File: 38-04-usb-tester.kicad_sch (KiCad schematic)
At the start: 63 parts, among them J1 Conn_1x05, J2 USB_C_12401832E402A, J3 USB_C_12401832E402A, J4 USB_Micro-B_KH-MICRO5P-JN, J5 USB_Mini-B_U-M-M5DD-W-1, J6 USB3_A_HC-USB3.0-L168-WP, SW1 SW_SPDT, SW2 ZX-1.27BM-4PSMD, U1 STM32C031K6Tx

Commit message: added defaults for jlpcb, fixed usb schematics
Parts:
- R1, R2, R3: footprint Resistor_SMD:R_0201_0603Metric -> Resistor_SMD:R_0805_2012Metric_Pad1.20x1.40mm_HandSolder; JLPCB_MPN 🔶TBD -> DNP; JLPCB_Mfg 🔶TBD -> DNP; JLPCB_Part_No 🔶TBD -> DNP; JLPCB_Price 🔶TBD -> DNP
- R5: footprint Resistor_SMD:R_0201_0603Metric -> Resistor_SMD:R_0805_2012Metric_Pad1.20x1.40mm_HandSolder
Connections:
- net GND: no longer J3.A1 (GND_A1), J3.A12 (GND_A12), J3.B12 (GND_B12)
- net B_GND_B1 renamed B_GND_A1
- net B_GND_A1: now also J3.A1 (GND_A1), J3.A12 (GND_A12), J3.B12 (GND_B12)
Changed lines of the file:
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@@
   (junction (at 334.01 184.785) (diameter 0) (color 0 0 0 0)
   )
+  (junction (at 128.27 173.99) (diameter 0) (color 0 0 0 0)
+  )
   (junction (at 31.75 180.975) (diameter 0) (color 0 0 0 0)
   )
+  (junction (at 128.27 171.45) (diameter 0) (color 0 0 0 0)
+  )
   (junction (at 223.52 57.785) (diameter 0) (color 0 0 0 0)
   )
@@
     (stroke (width 0) (type default))
   )
+  (wire (pts (xy 128.27 171.45) (xy 128.27 168.91))
+    (stroke (width 0) (type default))
+  )
   (wire (pts (xy 281.305 185.42) (xy 274.955 185.42))
     (stroke (width 0) (type default))
@@
     (stroke (width 0) (type default))
   )
+  (wire (pts (xy 128.27 173.99) (xy 139.065 173.99))
+    (stroke (width 0) (type default))
+  )
   (wire (pts (xy 29.845 126.365) (xy 41.275 126.365))
     (stroke (width 0) (type default))
   )
+  (wire (pts (xy 116.205 168.91) (xy 128.27 168.91))
+    (stroke (width 0) (type default))
+  )
   (wire (pts (xy 60.96 234.95) (xy 60.96 231.775))
     (stroke (width 0) (type default))
@@
     (stroke (width 0) (type default))
   )
+  (wire (pts (xy 128.27 171.45) (xy 128.27 173.99))
+    (stroke (width 0) (type default))
+  )
   (wire (pts (xy 203.835 142.24) (xy 203.835 144.78))
     (stroke (width 0) (type default))
@@
     (stroke (width 0) (type default))
   )
+  (wire (pts (xy 116.205 171.45) (xy 128.27 171.45))
+    (stroke (width 0) (type default))
+  )
   (wire (pts (xy 130.81 32.385) (xy 143.51 32.385))
     (stroke (width 0) (type default))
@@
     (stroke (width 0) (type default))
   )
+  (wire (pts (xy 116.205 173.99) (xy 128.27 173.99))
+    (stroke (width 0) (type default))
+  )
   (wire (pts (xy 215.9 139.7) (xy 218.44 139.7))
     (stroke (width 0) (type default))
@@
     (effects (font (size 1.27 1.27)) (justify right bottom))
   )
+  (label "B_GND_B1" (at 139.065 173.99 180) (fields_autoplaced)
+    (effects (font (size 1.27 1.27)) (justify right bottom))
+  )
   (label "A_SBU2" (at 88.9 118.745 180) (fields_autoplaced)
     (effects (font (size 1.27 1.27)) (justify right bottom))
@@
     (effects (font (size 1.27 1.27)) (justify left bottom))
   )
+  (label "B_GND_B12" (at 116.205 173.99 0) (fields_autoplaced)
+    (effects (font (size 1.27 1.27)) (justify left bottom))
+  )
   (label "ID" (at 285.115 191.77 180) (fields_autoplaced)
     (effects (font (size 1.27 1.27)) (justify right bottom))
@@
     (effects (font (size 1.27 1.27)) (justify left bottom))
   )
+  (label "B_GND_A1" (at 116.205 168.91 0) (fields_autoplaced)
+    (effects (font (size 1.27 1.27)) (justify left bottom))
+  )
   (label "CC_bb" (at 260.35 165.735 180) (fields_autoplaced)
     (effects (font (size 1.27 1.27)) (justify right bottom))
@@
     (effects (font (size 1.27 1.27)) (justify left bottom))
   )
+  (label "B_GND_A12" (at 116.205 171.45 0) (fields_autoplaced)
+    (effects (font (size 1.27 1.27)) (justify left bottom))
+  )
   (label "B_CC1_SENS" (at 184.785 42.545 180) (fields_autoplaced)
     (effects (font (size 1.27 1.27)) (justify right bottom))
@@
     )
   )
-  (symbol (lib_name "GND_1") (lib_id "power:GND") (at 135.255 157.48 0) (unit 1)
-    (in_bom yes) (on_board yes) (dnp no)
-    (property "Reference" "#PWR020" (at 135.255 163.83 0)
-      (effects (font (size 1.27 1.27)) hide)
-    )
-    (property "Value" "GND" (at 135.255 161.29 0)
-      (effects (font (size 1.27 1.27)))
-    )
-    (property "Footprint" "" (at 135.255 157.48 0)
-      (effects (font (size 1.27 1.27)) hide)
-    )
-    (property "Datasheet" "" (at 135.255 157.48 0)
-      (effects (font (size 1.27 1.27)) hide)
-    )
-    (pin "1")
-    (instances
-      (project "38-04-usb-tester"
-        (path "/450ad4bb-cada-4792-8f0e-c28850095e87"
-          (reference "#PWR020") (unit 1)
-        )
-      )
-    )
-  )
   (symbol (lib_id "01B-UserSchematics:SW_DIP_x04_Separated") (at 196.85 163.195 90) (unit 2)
     (in_bom yes) (on_board yes) (dnp no)
@@
     )
   )
-  (symbol (lib_name "GND_1") (lib_id "power:GND") (at 198.12 129.54 90) (unit 1)
-    (in_bom yes) (on_board yes) (dnp no)
-    (property "Reference" "#PWR018" (at 204.47 129.54 0)
-      (effects (font (size 1.27 1.27)) hide)
-    )
-    (property "Value" "GND" (at 201.295 129.54 90)
-      (effects (font (size 1.27 1.27)) (justify right))
-    )
-    (property "Footprint" "" (at 198.12 129.54 0)
-      (effects (font (size 1.27 1.27)) hide)
-    )
-    (property "Datasheet" "" (at 198.12 129.54 0)
-      (effects (font (size 1.27 1.27)) hide)
-    )
-    (pin "1")
-    (instances
-      (project "38-04-usb-tester"
-        (path "/450ad4bb-cada-4792-8f0e-c28850095e87"
-          (reference "#PWR018") (unit 1)
-        )
-      )
-    )
-  )
   (symbol (lib_id "Mechanical:MountingHole_Pad") (at 133.985 205.74 90) (mirror x) (unit 1)
     (in_bom yes) (on_board yes) (dnp no)
@@
       (effects (font (size 1.27 1.27)))
     )
-    (property "Footprint" "Resistor_SMD:R_0201_0603Metric" (at 193.04 41.783 90)
+    (property "Footprint" "Resistor_SMD:R_0805_2012Metric_Pad1.20x1.40mm_HandSolder" (at 193.04 41.783 90)
       (effects (font (size 1.27 1.27)) hide)
     )
@@
       (effects (font (size 1.27 1.27)) hide)
     )
-    (property "JLPCB_MPN" "🔶TBD" (at 193.04 40.005 0)
+    (property "JLPCB_MPN" "DNP" (at 193.04 40.005 0)
       (effects (font (size 1.27 1.27)) hide)
     )
-    (property "JLPCB_Mfg" "🔶TBD" (at 193.04 40.005 0)
+    (property "JLPCB_Mfg" "DNP" (at 193.04 40.005 0)
       (effects (font (size 1.27 1.27)) hide)
     )
-    (property "JLPCB_Part_No" "🔶TBD" (at 193.04 40.005 0)
+    (property "JLPCB_Part_No" "DNP" (at 193.04 40.005 0)
       (effects (font (size 1.27 1.27)) hide)
     )
@@
       (effects (font (size 1.27 1.27)) hide)
     )
-    (property "JLPCB_Price" "🔶TBD" (at 193.04 40.005 0)
+    (property "JLPCB_Price" "DNP" (at 193.04 40.005 0)
+      (effects (font (size 1.27 1.27)) hide)
+    )
+    (property "Description" "GND Pulldowns" (at 193.04 40.005 0)
       (effects (font (size 1.27 1.27)) hide)
     )
@@
     )
   )
-  (symbol (lib_name "GND_1") (lib_id "power:GND") (at 135.255 129.54 270) (unit 1)
-    (in_bom yes) (on_board yes) (dnp no)
-    (property "Reference" "#PWR017" (at 128.905 129.54 0)
-      (effects (font (size 1.27 1.27)) hide)
-    )
-    (property "Value" "GND" (at 132.715 129.54 90)
-      (effects (font (size 1.27 1.27)) (justify right))
-    )
-    (property "Footprint" "" (at 135.255 129.54 0)
-      (effects (font (size 1.27 1.27)) hide)
-    )
-    (property "Datasheet" "" (at 135.255 129.54 0)
-      (effects (font (size 1.27 1.27)) hide)
-    )
-    (pin "1")
-    (instances
-      (project "38-04-usb-tester"
-        (path "/450ad4bb-cada-4792-8f0e-c28850095e87"
-          (reference "#PWR017") (unit 1)
-        )
-      )
-    )
-  )
   (symbol (lib_id "Mechanical:MountingHole_Pad") (at 167.005 111.76 180) (unit 1)
     (in_bom yes) (on_board yes) (dnp no)
@@
       (effects (font (size 1.27 1.27)))
     )
-    (property "Footprint" "Resistor_SMD:R_0201_0603Metric" (at 193.04 39.243 90)
+    (property "Footprint" "Resistor_SMD:R_0805_2012Metric_Pad1.20x1.40mm_HandSolder" (at 193.04 39.243 90)
       (effects (font (size 1.27 1.27)) hide)
     )
@@
       (effects (font (size 1.27 1.27)) hide)
     )
-    (property "JLPCB_MPN" "🔶TBD" (at 193.04 37.465 0)
+    (property "JLPCB_MPN" "DNP" (at 193.04 37.465 0)
       (effects (font (size 1.27 1.27)) hide)
     )
-    (property "JLPCB_Mfg" "🔶TBD" (at 193.04 37.465 0)
+    (property "JLPCB_Mfg" "DNP" (at 193.04 37.465 0)
       (effects (font (size 1.27 1.27)) hide)
     )
-    (property "JLPCB_Part_No" "🔶TBD" (at 193.04 37.465 0)
+    (property "JLPCB_Part_No" "DNP" (at 193.04 37.465 0)
       (effects (font (size 1.27 1.27)) hide)
     )
@@
       (effects (font (size 1.27 1.27)) hide)
     )
-    (property "JLPCB_Price" "🔶TBD" (at 193.04 37.465 0)
+    (property "JLPCB_Price" "DNP" (at 193.04 37.465 0)
+      (effects (font (size 1.27 1.27)) hide)
+    )
+    (property "Description" "GND Pulldowns" (at 193.04 37.465 0)
       (effects (font (size 1.27 1.27)) hide)
     )
@@
       (effects (font (size 1.27 1.27)))
     )
-    (property "Footprint" "Resistor_SMD:R_0201_0603Metric" (at 193.04 36.703 90)
+    (property "Footprint" "Resistor_SMD:R_0805_2012Metric_Pad1.20x1.40mm_HandSolder" (at 193.04 36.703 90)
       (effects (font (size 1.27 1.27)) hide)
     )
@@
       (effects (font (size 1.27 1.27)) hide)
     )
-    (property "JLPCB_MPN" "🔶TBD" (at 193.04 34.925 0)
+    (property "JLPCB_MPN" "DNP" (at 193.04 34.925 0)
       (effects (font (size 1.27 1.27)) hide)
     )
-    (property "JLPCB_Mfg" "🔶TBD" (at 193.04 34.925 0)
+    (property "JLPCB_Mfg" "DNP" (at 193.04 34.925 0)
       (effects (font (size 1.27 1.27)) hide)
     )
-    (property "JLPCB_Part_No" "🔶TBD" (at 193.04 34.925 0)
+    (property "JLPCB_Part_No" "DNP" (at 193.04 34.925 0)
       (effects (font (size 1.27 1.27)) hide)
     )
@@
       (effects (font (size 1.27 1.27)) hide)
     )
-    (property "JLPCB_Price" "🔶TBD" (at 193.04 34.925 0)
+    (property "JLPCB_Price" "DNP" (at 193.04 34.925 0)
+      (effects (font (size 1.27 1.27)) hide)
+    )
+    (property "Description" "GND Pulldowns" (at 193.04 34.925 0)
       (effects (font (size 1.27 1.27)) hide)
     )
@@
       (effects (font (size 1.27 1.27)))
     )
-    (property "Footprint" "Resistor_SMD:R_0201_0603Metric" (at 143.51 110.998 90)
+    (property "Footprint" "Resistor_SMD:R_0805_2012Metric_Pad1.20x1.40mm_HandSolder" (at 143.51 110.998 90)
       (effects (font (size 1.27 1.27)) hide)
     )

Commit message: started routing
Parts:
- SW2: JLPCB_MPN ZX-1.27BM-4PSMD -> SP-04P; JLPCB_Mfg Megastar -> DEALON; JLPCB_Part_No C7527753 -> C5160896; JLPCB_Price (none) -> $0.49; JLPCB_URL https://jlcpcb.com/partdetail/Megastar-ZX_1_27BM4PSMD/C7527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 -> https://jlcpcb.com/partdetail/Dealon-SP04P/C5160896
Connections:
- net B_GND_A1: now also J4.5 (GND), J5.5 (GND)
- net GND: no longer J4.5 (GND), J5.5 (GND)
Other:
- note added: "Open SW2 A-D to test A and B side VBUS to GND, or Rp, Rd, Ra"
- note removed: "Open SW3 A-D to test A and B side VBUS to GND, or Rp, Rd, Ra"

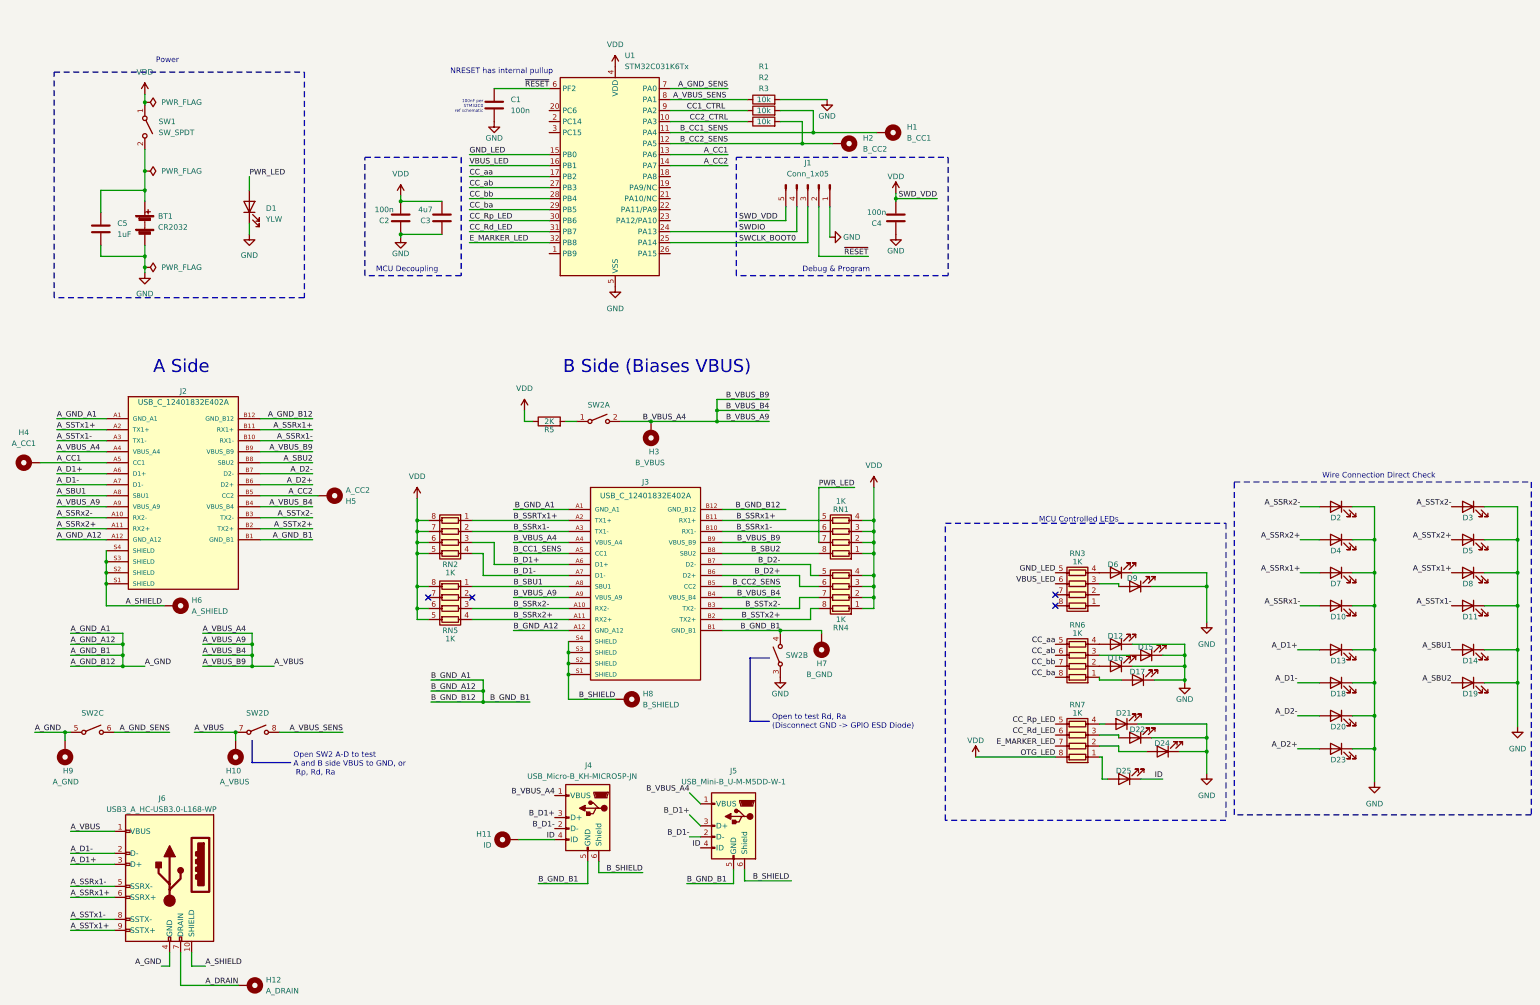
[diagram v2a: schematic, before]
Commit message: routing LEDs, started USB B side
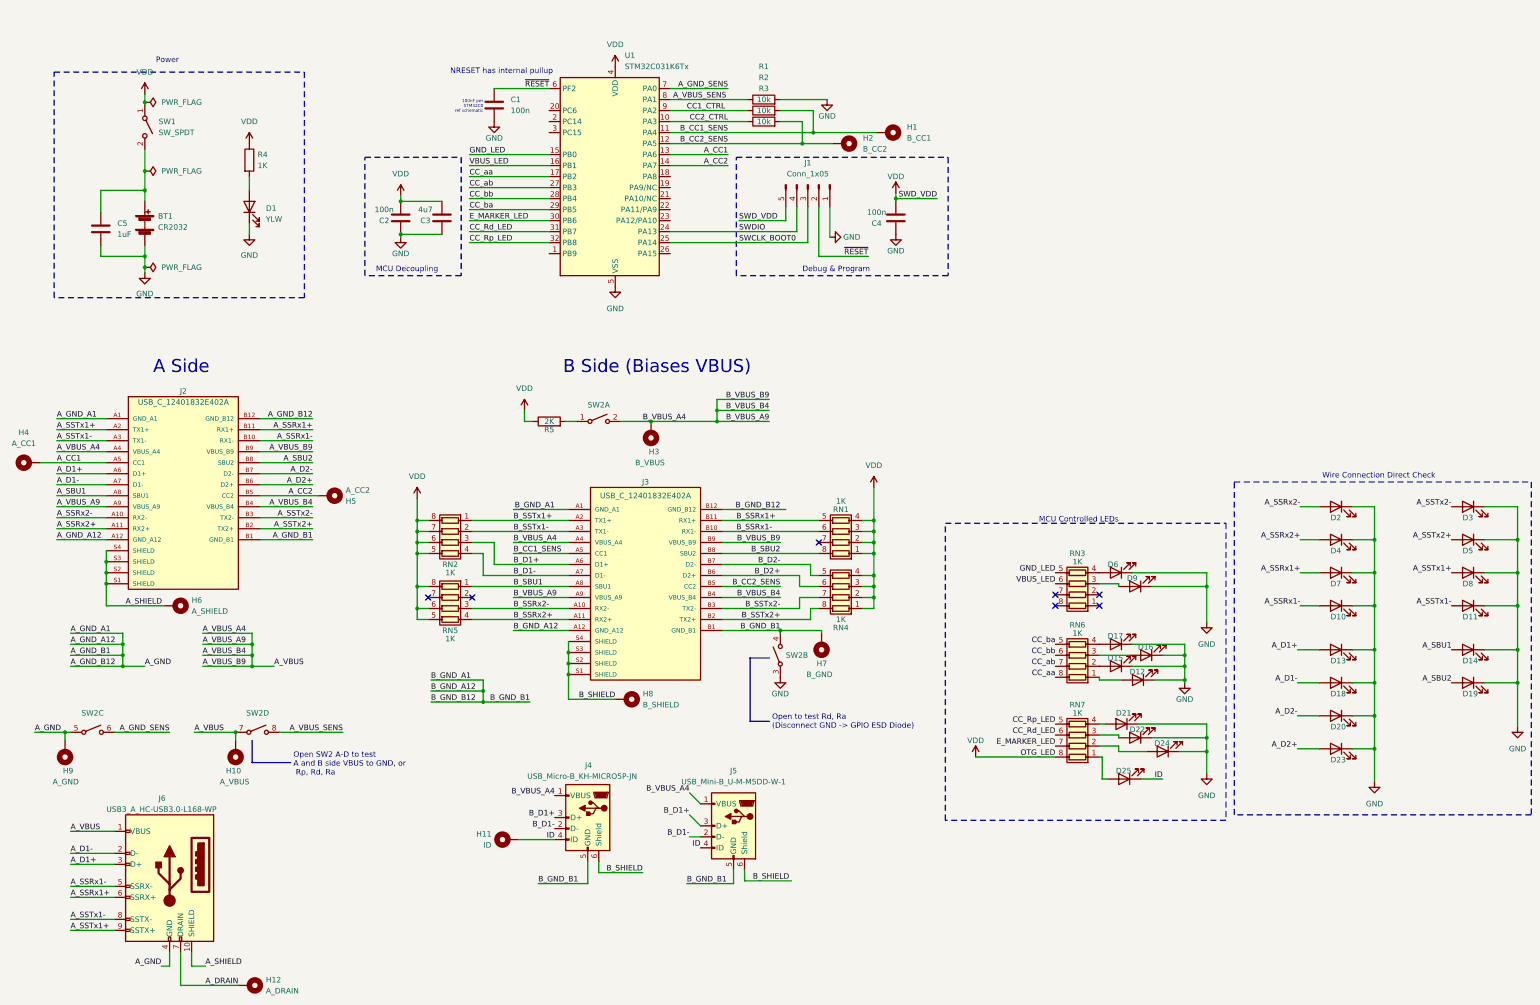
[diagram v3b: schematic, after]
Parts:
- added R4: 1K, Resistor_SMD:R_0805_2012Metric_Pad1.20x1.40mm_HandSolder, symbol Device:R
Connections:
- net B_SSRx1-: no longer J3.A3 (TX1-), RN2.2 (R2.1)
- net CC_Rp_LED: now also U1.32 (PB8); no longer U1.30 (PB6)
- net CC_aa: now also RN6.8 (R1.2); no longer RN6.5 (R4.2)
- net CC_ab: now also RN6.7 (R2.2); no longer RN6.6 (R3.2)
- net CC_ba: now also RN6.5 (R4.2); no longer RN6.8 (R1.2)
- net CC_bb: now also RN6.6 (R3.2); no longer RN6.7 (R2.2)
- net E_MARKER_LED: now also U1.30 (PB6); no longer U1.32 (PB8)
- net VCC: now also R4.1
- net at D16.2 (A): now also RN6.3 (R3.1); no longer RN6.2 (R2.1)
- net at D17.2 (A): now also RN6.4 (R4.1); no longer RN6.1 (R1.1)
- net at D15.2 (A): now also RN6.2 (R2.1); no longer RN6.3 (R3.1)
- net at D12.2 (A): now also RN6.1 (R1.1); no longer RN6.4 (R4.1)
- net B_SSRTx1+ renamed B_SSTx1+
- net PWR_LED: no longer names the net of RN1.7 (R2.2)
- net PWR_LED: no longer D1.2 (A)
- new net: D1.2 (A), R4.2
- new net B_SSTx1-: J3.A3 (TX1-), RN2.2 (R2.1)
- no-connect marks 4 -> 7
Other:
- moved on the sheet: D12, D15, D16, D17

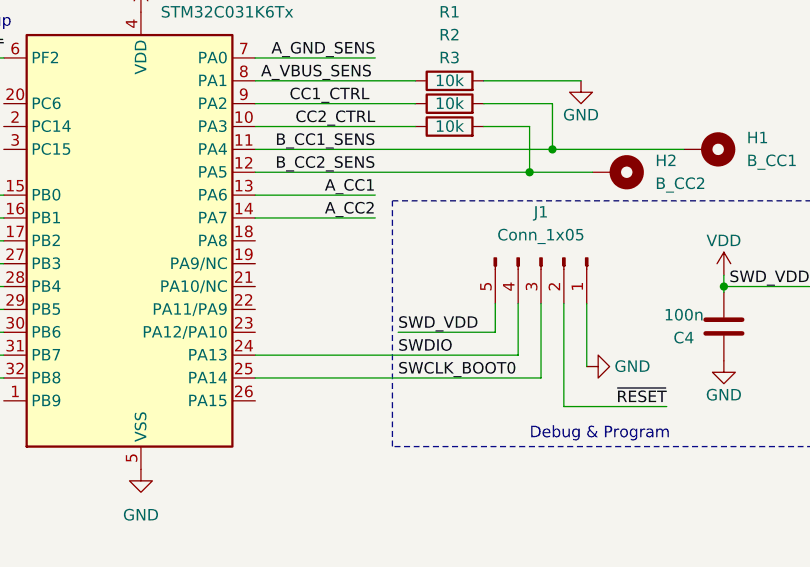
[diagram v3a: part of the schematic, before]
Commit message: via size change refactoring DRC errors
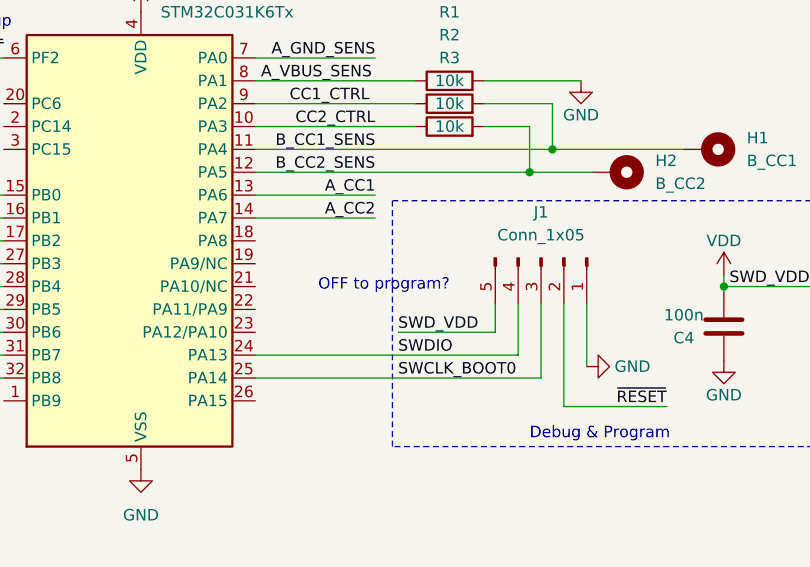
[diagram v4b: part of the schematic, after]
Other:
- note added: "OFF to program?"
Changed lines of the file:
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@@
+    (effects (font (size 1.27 1.27)) (justify left bottom))
+  )
+  (text "OFF to program? " (at 178.435 58.42 0)
     (effects (font (size 1.27 1.27)) (justify left bottom))
   )
